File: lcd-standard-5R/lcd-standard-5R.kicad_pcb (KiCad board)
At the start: 4 copper layers, 137.4 x 82.6 mm, 156 parts, among them J1 USB_C_Receptacle_USB2.0_16P, J2 SWD, J3 Conn_ARM_JTAG_SWD_10, J4 Micro_SD_Card_Det1, J6 Conn_01x40_MountingPin, J7 Conn_01x02_MountingPin, J8 Serial, Q1 DMG3415, Q2 MMBT3904, Q3 MMBT3904, Q4 MMBT3904, SW1 SW_Push, SW2 SW_Push, SW3 BOOT0, SW4 RST, U1 siplex-som-s16, U2 AMS1117-3.3, U3 STM32H743ZITx, U4 MT48LC16M16A2P, U5 MT25Q, U6 CAT24C256, U7 XPT2046TS, U8 TPS61169, U9 MAX98357A, Y1 25MHz, Y2 32.768KHz

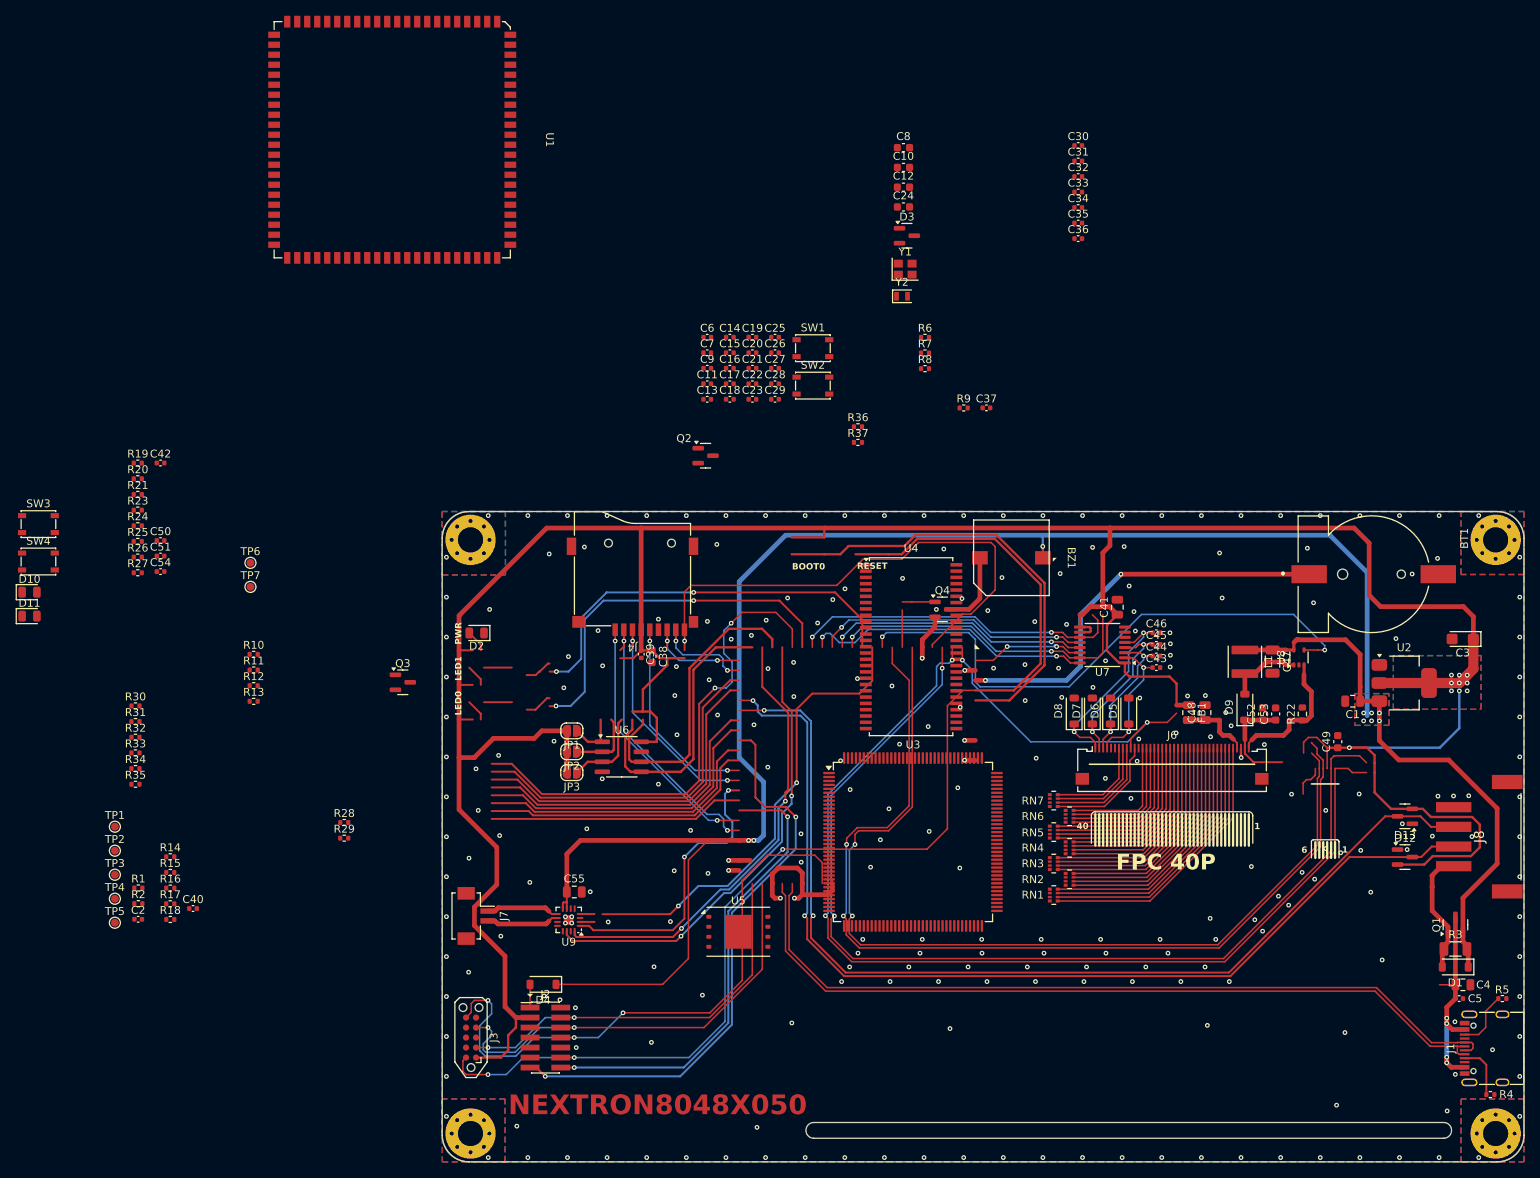
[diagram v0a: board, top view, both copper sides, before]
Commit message: Change MCU to STM32H743
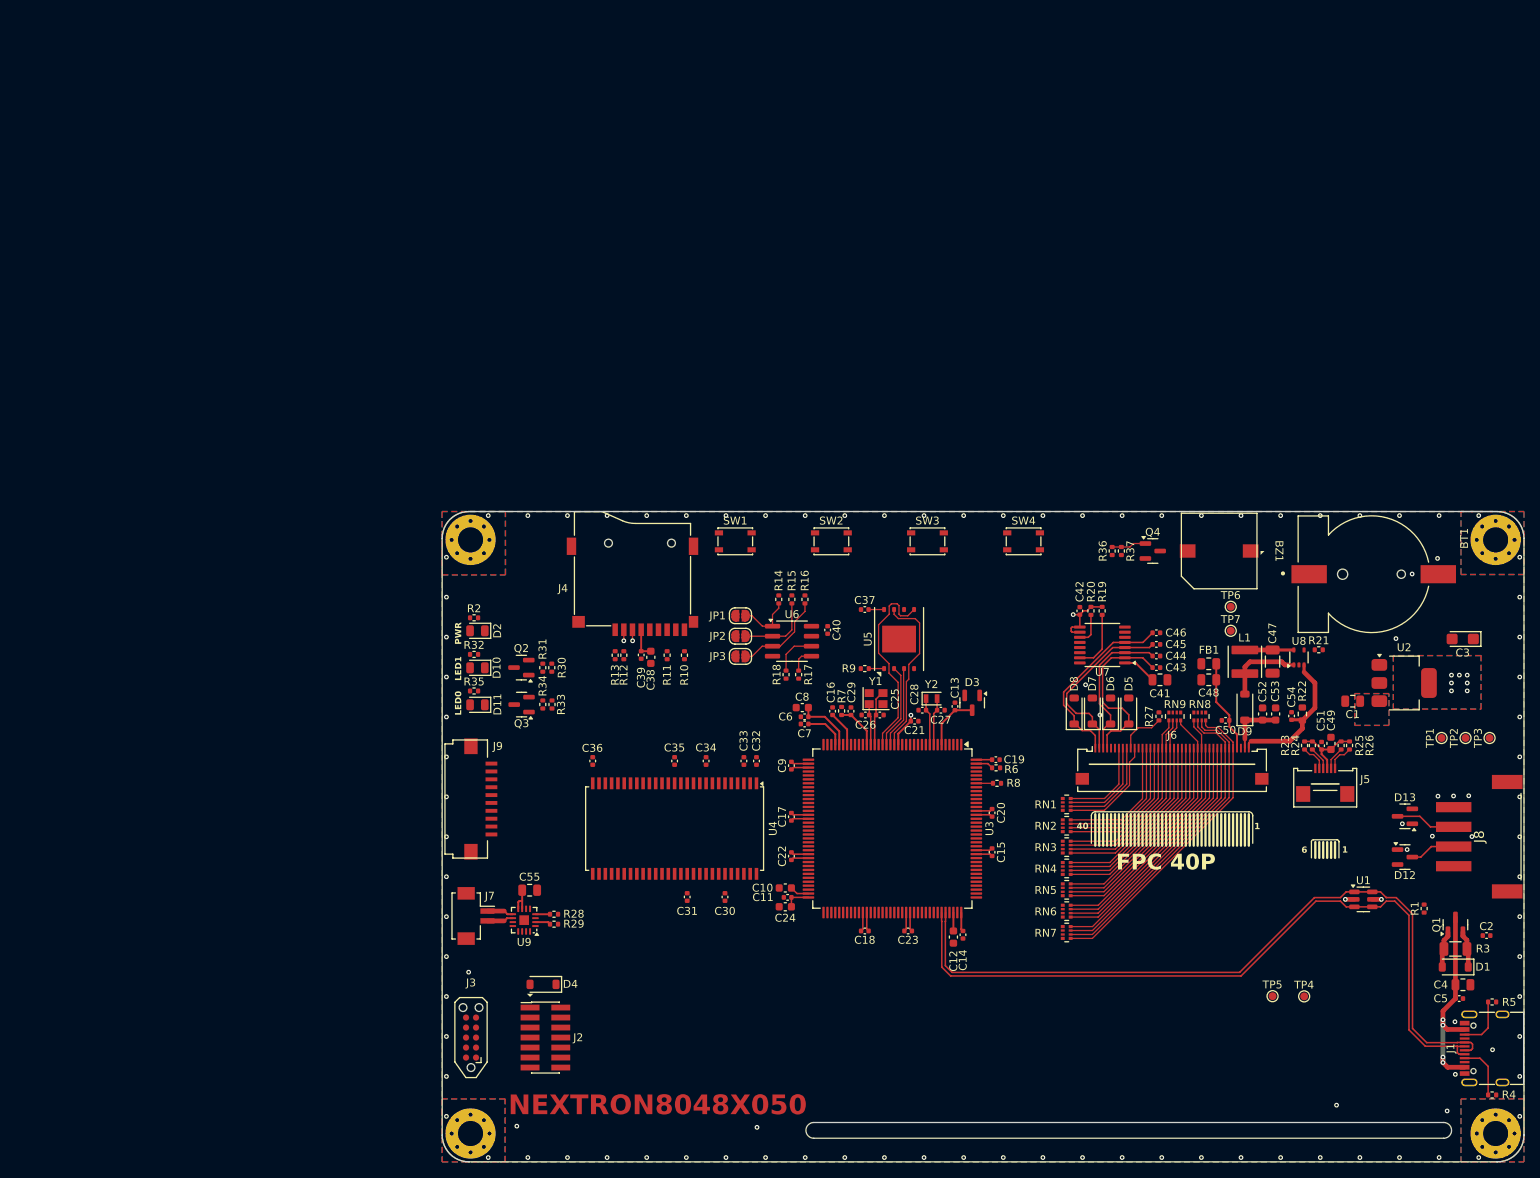
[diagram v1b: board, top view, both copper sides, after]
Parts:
- added J5: Conn_01x06_MountingPin, Connector_FPC:Conn_FPC_6P_0.5mm_XUNPU_FPC-05FB-6PH20, F.Cu at (188.6, 86.5)
- added J9: AUX_IO, Connector_FPC:Conn_FPC_10P_1mm_G-SWITCH_GT-F1008SR20-10SMT01, F.Cu at (82.7, 90.4)
- added RN8: 10K, Resistor_SMD:R_Array_Convex_4x0402, F.Cu at (172.6, 79.9)
- added RN9: 10K, Resistor_SMD:R_Array_Convex_4x0402, F.Cu at (169.5, 79.9)
- U1: value siplex-som-s16 -> USBLC6-2SC6; footprint siplex:siplex-som-s16 -> Package_TO_SOT_SMD:SOT-23-6
- moved TP3 175.5 mm to (209.5, 82.7), turned to 90 degrees
- moved TP2 172.1 mm to (206.4, 82.7), turned to 90 degrees
- moved C2 171.3 mm to (209.1, 107.8)
- moved TP1 168.9 mm to (203.4, 82.7), turned to 90 degrees
- moved R1 163.3 mm to (201.1, 104.3), turned to 90 degrees
- moved U1 156.6 mm to (193.4, 103.2), turned to 0 degrees
- moved R26 155.8 mm to (191.7, 83.6), turned to -90 degrees
- moved R25 155.0 mm to (190.6, 83.6), turned to -90 degrees
- moved R24 151.8 mm to (186.9, 83.6), turned to 90 degrees
- moved TP4 151.6 mm to (185.9, 115.5)
- moved R21 151.3 mm to (187.8, 71.5)
- moved R23 151.2 mm to (186.0, 83.6), turned to 90 degrees
- moved C51 149.4 mm to (188.1, 83.7), turned to 90 degrees
- moved TP5 147.3 mm to (181.9, 115.5)
- moved C54 144.8 mm to (184.3, 79.9), turned to 90 degrees
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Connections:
- net /DISPLAY/TP_BUSY renamed /DISPLAY/RTP_BUSY
- net /DISPLAY/TP_CLK renamed /DISPLAY/RTP_CLK
- net /DISPLAY/TP_CS renamed /DISPLAY/RTP_CS
- net /DISPLAY/TP_IRQ renamed /DISPLAY/RTP_IRQ
- net /DISPLAY/TP_MISO renamed /DISPLAY/RTP_MISO
- net /DISPLAY/TP_MOSI renamed /DISPLAY/RTP_MOSI
- J1 pad A6: /USB_DP -> /MCU/USB_D+
- J1 pad A7: /USB_DN -> /MCU/USB_D-
- J1 pad B6: /USB_DP -> /MCU/USB_D+
- J1 pad B7: /USB_DN -> /MCU/USB_D-
- J4 pad 1: /MEMORY_SD_CARD/DAT2 -> /MEMORY_SD_CARD/SD_DAT2
- J4 pad 2: /MEMORY_SD_CARD/DAT3 -> /MEMORY_SD_CARD/SD_DAT3
- J4 pad 3: /MEMORY_SD_CARD/CMD -> /MEMORY_SD_CARD/SD_CMD
- J4 pad 5: /MEMORY_SD_CARD/CLK -> /MEMORY_SD_CARD/SD_CLK
- J4 pad 7: /MEMORY_SD_CARD/DAT0 -> /MEMORY_SD_CARD/SD_DAT0
- J4 pad 8: /MEMORY_SD_CARD/DAT1 -> /MEMORY_SD_CARD/SD_DAT1
- J6 pad 11: /DISPLAY/LCD_CLK -> Net-(J6-Pin_11)
- J6 pad 13: /DISPLAY/LCD_B7 -> Net-(J6-Pin_13)
- J6 pad 14: /DISPLAY/LCD_B6 -> Net-(J6-Pin_14)
- J6 pad 15: /DISPLAY/LCD_B5 -> Net-(J6-Pin_15)
- J6 pad 16: /DISPLAY/LCD_B4 -> Net-(J6-Pin_16)
- J6 pad 17: /DISPLAY/LCD_B3 -> Net-(J6-Pin_17)
- J6 pad 18: /DISPLAY/LCD_B2 -> /DISPLAY/B2
- J6 pad 19: /DISPLAY/LCD_B1 -> /DISPLAY/B1
- J6 pad 20: /DISPLAY/LCD_B0 -> /DISPLAY/B0
- J6 pad 21: /DISPLAY/LCD_G7 -> Net-(J6-Pin_21)
- J6 pad 22: /DISPLAY/LCD_G6 -> Net-(J6-Pin_22)
- J6 pad 23: /DISPLAY/LCD_G5 -> Net-(J6-Pin_23)
- J6 pad 24: /DISPLAY/LCD_G4 -> Net-(J6-Pin_24)
- J6 pad 25: /DISPLAY/LCD_G3 -> Net-(J6-Pin_25)
- J6 pad 26: /DISPLAY/LCD_G2 -> Net-(J6-Pin_26)
- J6 pad 27: /DISPLAY/LCD_G1 -> /DISPLAY/G1
- J6 pad 28: /DISPLAY/LCD_G0 -> /DISPLAY/G0
- J6 pad 29: /DISPLAY/LCD_R7 -> Net-(J6-Pin_29)
- J6 pad 30: /DISPLAY/LCD_R6 -> Net-(J6-Pin_30)
- J6 pad 31: /DISPLAY/LCD_R5 -> Net-(J6-Pin_31)
- J6 pad 32: /DISPLAY/LCD_R4 -> Net-(J6-Pin_32)
- J6 pad 33: /DISPLAY/LCD_R3 -> Net-(J6-Pin_33)
- J6 pad 34: /DISPLAY/LCD_R2 -> /DISPLAY/R2
- J6 pad 35: /DISPLAY/LCD_R1 -> /DISPLAY/R1
- J6 pad 36: /DISPLAY/LCD_R0 -> /DISPLAY/R0
- J6 pad 7: /DISPLAY/LCD_DE -> Net-(J6-Pin_7)
- J6 pad 8: /DISPLAY/LCD_VSYNC -> Net-(J6-Pin_8)
- J6 pad 9: /DISPLAY/LCD_HSYNC -> Net-(J6-Pin_9)
- R11 pad 2: /MEMORY_SD_CARD/DAT0 -> /MEMORY_SD_CARD/SD_DAT0
- R12 pad 2: /MEMORY_SD_CARD/CMD -> /MEMORY_SD_CARD/SD_CMD
- R13 pad 2: /MEMORY_SD_CARD/DAT3 -> /MEMORY_SD_CARD/SD_DAT3
- R23 pad 1: /DISPLAY/TP_INT -> /DISPLAY/CTP_INT
- R24 pad 1: /DISPLAY/TP_WAKE -> /DISPLAY/CTP_WAKE
- R25 pad 2: /DISPLAY/TP_SDA -> /DISPLAY/CTP_SDA
- R26 pad 2: /DISPLAY/TP_SCL -> /DISPLAY/CTP_SCL
- RN1 pad 1: /LCD_R0 -> /DISPLAY/LCD_DE
- RN1 pad 2: /LCD_R1 -> /DISPLAY/LCD_VSYNC
- RN1 pad 3: /LCD_R2 -> /DISPLAY/LCD_HSYNC
- RN1 pad 4: /LCD_R3 -> /DISPLAY/LCD_CLK
- RN1 pad 5: /R3 -> Net-(J6-Pin_11)
- RN1 pad 6: /R2 -> Net-(J6-Pin_9)
- RN1 pad 7: /R1 -> Net-(J6-Pin_8)
- RN1 pad 8: Net-(RN1-R1.2) -> Net-(J6-Pin_7)
- RN2 pad 1: /LCD_R4 -> Net-(J6-Pin_16)
- RN2 pad 2: /LCD_R5 -> Net-(J6-Pin_15)
- RN2 pad 3: /LCD_R6 -> Net-(J6-Pin_14)
- RN2 pad 4: /LCD_R7 -> Net-(J6-Pin_13)
- RN2 pad 5: /R7 -> /DISPLAY/LCD_B7
- RN2 pad 6: /R6 -> /DISPLAY/LCD_B6
- RN2 pad 7: /R5 -> /DISPLAY/LCD_B5
- RN2 pad 8: /R4 -> /DISPLAY/LCD_B4
- RN3 pad 1: /LCD_G0 -> /DISPLAY/B0
- RN3 pad 2: /LCD_G1 -> /DISPLAY/B1
- RN3 pad 3: /LCD_G2 -> /DISPLAY/B2
- RN3 pad 4: /LCD_G3 -> Net-(J6-Pin_17)
- RN3 pad 5: /G3 -> /DISPLAY/LCD_B3
- RN3 pad 6: /G2 -> /DISPLAY/LCD_B2
- RN3 pad 7: /G1 -> /DISPLAY/LCD_B1
- RN3 pad 8: /G0 -> /DISPLAY/LCD_B0
- RN4 pad 1: /LCD_G4 -> Net-(J6-Pin_24)
- RN4 pad 2: /LCD_G5 -> Net-(J6-Pin_23)
- RN4 pad 3: /LCD_G6 -> Net-(J6-Pin_22)
- RN4 pad 4: /LCD_G7 -> Net-(J6-Pin_21)
- RN4 pad 5: /G7 -> /DISPLAY/LCD_G7
- RN4 pad 6: /G6 -> /DISPLAY/LCD_G6
- RN4 pad 7: /G5 -> /DISPLAY/LCD_G5
- RN4 pad 8: /G4 -> /DISPLAY/LCD_G4
- RN5 pad 1: /LCD_B0 -> /DISPLAY/G0
- RN5 pad 2: /LCD_B1 -> /DISPLAY/G1
- RN5 pad 3: /LCD_B2 -> Net-(J6-Pin_26)
- RN5 pad 4: /LCD_B3 -> Net-(J6-Pin_25)
- RN5 pad 5: /B3 -> /DISPLAY/LCD_G3
- RN5 pad 6: /B2 -> /DISPLAY/LCD_G2
- RN5 pad 7: /B1 -> /DISPLAY/LCD_G1
- RN5 pad 8: /B0 -> /DISPLAY/LCD_G0
- RN6 pad 1: /LCD_B4 -> Net-(J6-Pin_32)
- RN6 pad 2: /LCD_B5 -> Net-(J6-Pin_31)
- RN6 pad 3: /LCD_B6 -> Net-(J6-Pin_30)
- RN6 pad 4: /LCD_B7 -> Net-(J6-Pin_29)
- RN6 pad 5: /B7 -> /DISPLAY/LCD_R7
- RN6 pad 6: /B6 -> /DISPLAY/LCD_R6
- RN6 pad 7: /B5 -> /DISPLAY/LCD_R5
- RN6 pad 8: /B4 -> /DISPLAY/LCD_R4
- RN7 pad 1: /LCD_CLK -> /DISPLAY/R0
- RN7 pad 2: /LCD_HSYNC -> /DISPLAY/R1
- RN7 pad 3: /LCD_VSYNC -> /DISPLAY/R2
- RN7 pad 4: /LCD_DE -> Net-(J6-Pin_33)
- RN7 pad 5: Net-(RN7-R4.2) -> /DISPLAY/LCD_R3
- RN7 pad 6: Net-(RN7-R3.2) -> /DISPLAY/LCD_R2
- RN7 pad 7: Net-(RN7-R2.2) -> /DISPLAY/LCD_R1
- RN7 pad 8: Net-(RN7-R1.2) -> /DISPLAY/LCD_R0
- U1 pad 1: /LCD_RST -> /MCU/USB_D+
- U1 pad 2: /TP_SCL -> GND
- U1 pad 3: /TP_SDA -> /MCU/USB_D-
- U1 pad 4: /SD_DET -> /MCU/USB_D-
- U1 pad 5: GND -> VBUS
- U1 pad 6: /TP_INT -> /MCU/USB_D+
- U3 pad 123: /MCU/SD_CMD -> /MEMORY_SD_CARD/SD_CMD
- U3 pad 133: /MCU/SD_DAT2 -> /MEMORY_SD_CARD/SD_DAT2
- U3 pad 134: /MCU/SD_DAT3 -> /MEMORY_SD_CARD/SD_DAT3
- U3 pad 135: /MCU/SD_DET -> /MEMORY_SD_CARD/SD_DET
- U3 pad 136: /MCU/~{NOR_CS} -> /MEMORY_FLASH/~{NOR_CS}
- U3 pad 18: /MCU/NOR_D3 -> /MEMORY_FLASH/NOR_IO3
- U3 pad 19: /MCU/NOR_D2 -> /MEMORY_FLASH/NOR_IO2
- U3 pad 20: /MCU/NOR_D0 -> /MEMORY_FLASH/NOR_DO(IO1)
- U3 pad 21: /MCU/NOR_D1 -> /MEMORY_FLASH/NOR_DI(IO0)
- U3 pad 22: /MCU/LTDC_DE -> /DISPLAY/LCD_DE
- U3 pad 27: /MCU/SD_CLK -> /MEMORY_SD_CARD/SD_CLK
- U3 pad 3: /MCU/LCD_RESET -> /DISPLAY/LCD_RST
- U3 pad 40: /MCU/LTDC_VSYNC -> /DISPLAY/LCD_VSYNC
- U3 pad 43: /MCU/LCD_BLK -> /DISPLAY/LCD_BLK
- U3 pad 48: /MCU/NOR_CLK -> /MEMORY_FLASH/NOR_CLK
- U3 pad 75: /MCU/SD_DAT0 -> /MEMORY_SD_CARD/SD_DAT0
- U3 pad 76: /MCU/SD_DAT1 -> /MEMORY_SD_CARD/SD_DAT1
- U3 pad 92: /MCU/LTDC_CLK -> /DISPLAY/LCD_CLK
- U3 pad 96: /MCU/LTDC_HSYNC -> /DISPLAY/LCD_HSYNC
- U4 pad 10: /MEMORY_FMC/SDRAM_DQ5 -> /MCU/SDRAM_DQ5
- U4 pad 11: /MEMORY_FMC/SDRAM_DQ6 -> /MCU/SDRAM_DQ6
- U4 pad 13: /MEMORY_FMC/SDRAM_DQ7 -> /MCU/SDRAM_DQ7
- U4 pad 15: /MEMORY_FMC/SDRAM_LDQM -> /MCU/SDRAM_LDQM
- U4 pad 16: /MEMORY_FMC/~{SDRAM_WE} -> /MCU/~{SDRAM_WE}
- U4 pad 17: /MEMORY_FMC/~{SDRAM_CAS} -> /MCU/~{SDRAM_CAS}
- U4 pad 18: /MEMORY_FMC/~{SDRAM_RAS} -> /MCU/~{SDRAM_RAS}
- U4 pad 19: /MEMORY_FMC/~{SDRAM_CS} -> /MCU/~{SDRAM_CS}
- U4 pad 2: /MEMORY_FMC/SDRAM_DQ0 -> /MCU/SDRAM_DQ0
- U4 pad 20: /MEMORY_FMC/SDRAM_BA0 -> /MCU/SDRAM_BA0
- U4 pad 21: /MEMORY_FMC/SDRAM_BA1 -> /MCU/SDRAM_BA1
- U4 pad 22: /MEMORY_FMC/SDRAM_ADD10 -> /MCU/SDRAM_ADD10
- U4 pad 23: /MEMORY_FMC/SDRAM_ADD0 -> /MCU/SDRAM_ADD0
- U4 pad 24: /MEMORY_FMC/SDRAM_ADD1 -> /MCU/SDRAM_ADD1
- U4 pad 25: /MEMORY_FMC/SDRAM_ADD2 -> /MCU/SDRAM_ADD2
- U4 pad 26: /MEMORY_FMC/SDRAM_ADD3 -> /MCU/SDRAM_ADD3
- U4 pad 29: /MEMORY_FMC/SDRAM_ADD4 -> /MCU/SDRAM_ADD4
- U4 pad 30: /MEMORY_FMC/SDRAM_ADD5 -> /MCU/SDRAM_ADD5
- U4 pad 31: /MEMORY_FMC/SDRAM_ADD6 -> /MCU/SDRAM_ADD6
- U4 pad 32: /MEMORY_FMC/SDRAM_ADD7 -> /MCU/SDRAM_ADD7
- U4 pad 33: /MEMORY_FMC/SDRAM_ADD8 -> /MCU/SDRAM_ADD8
- U4 pad 34: /MEMORY_FMC/SDRAM_ADD9 -> /MCU/SDRAM_ADD9
- U4 pad 35: /MEMORY_FMC/SDRAM_ADD11 -> /MCU/SDRAM_ADD11
- U4 pad 36: /MEMORY_FMC/SDRAM_ADD12 -> /MCU/SDRAM_ADD12
- U4 pad 37: /MEMORY_FMC/SDRAM_CKE -> /MCU/SDRAM_CKE
- U4 pad 38: /MEMORY_FMC/SDRAM_CLK -> /MCU/SDRAM_CLK
- U4 pad 39: /MEMORY_FMC/SDRAM_UDQM -> /MCU/SDRAM_UDQM
- U4 pad 4: /MEMORY_FMC/SDRAM_DQ1 -> /MCU/SDRAM_DQ1
- U4 pad 42: /MEMORY_FMC/SDRAM_DQ8 -> /MCU/SDRAM_DQ8
- U4 pad 44: /MEMORY_FMC/SDRAM_DQ9 -> /MCU/SDRAM_DQ9
- U4 pad 45: /MEMORY_FMC/SDRAM_DQ10 -> /MCU/SDRAM_DQ10
- U4 pad 47: /MEMORY_FMC/SDRAM_DQ11 -> /MCU/SDRAM_DQ11
- U4 pad 48: /MEMORY_FMC/SDRAM_DQ12 -> /MCU/SDRAM_DQ12
- U4 pad 5: /MEMORY_FMC/SDRAM_DQ2 -> /MCU/SDRAM_DQ2
- U4 pad 50: /MEMORY_FMC/SDRAM_DQ13 -> /MCU/SDRAM_DQ13
- U4 pad 51: /MEMORY_FMC/SDRAM_DQ14 -> /MCU/SDRAM_DQ14
- U4 pad 53: /MEMORY_FMC/SDRAM_DQ15 -> /MCU/SDRAM_DQ15
- U4 pad 7: /MEMORY_FMC/SDRAM_DQ3 -> /MCU/SDRAM_DQ3
- U4 pad 8: /MEMORY_FMC/SDRAM_DQ4 -> /MCU/SDRAM_DQ4
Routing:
- net +3V3: track 410.3 -> 73.3 mm, vias 10 -> 9
- net VDD: track 279.0 -> 14.7 mm, vias 9 -> 0
- net /RESET: track 153.2 -> 0.00 mm, vias 3 -> 0
- net /TP_SCL: track 130.6 -> 0.00 mm, vias 2 -> 0
- net /TP_SDA: track 130.0 -> 0.00 mm, vias 2 -> 0
- net /TP_WAKE: track 123.5 -> 0.00 mm, vias 2 -> 0
- net /IO/SERIAL_TX: track 128.9 -> 5.81 mm, vias 2 -> 0
- net /IO/SERIAL_RX: track 129.7 -> 7.68 mm, vias 2 -> 0
- net /TP_INT: track 119.7 -> 0.00 mm, vias 2 -> 0
- net /USB_DP: track 102.1 -> 0.00 mm
- net /USB_DN: track 101.8 -> 0.00 mm
- net /MCU/USB_D+: track 0.00 -> 96.5 mm
- net /MCU/USB_D-: track 0.00 -> 96.3 mm
- net /MEMORY_FMC/SDRAM_UDQM: track 88.1 -> 0.00 mm
- net /MEMORY_FMC/SDRAM_CLK: track 79.1 -> 0.00 mm
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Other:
- board text removed: "BOOT0"
- board text removed: "RESET"

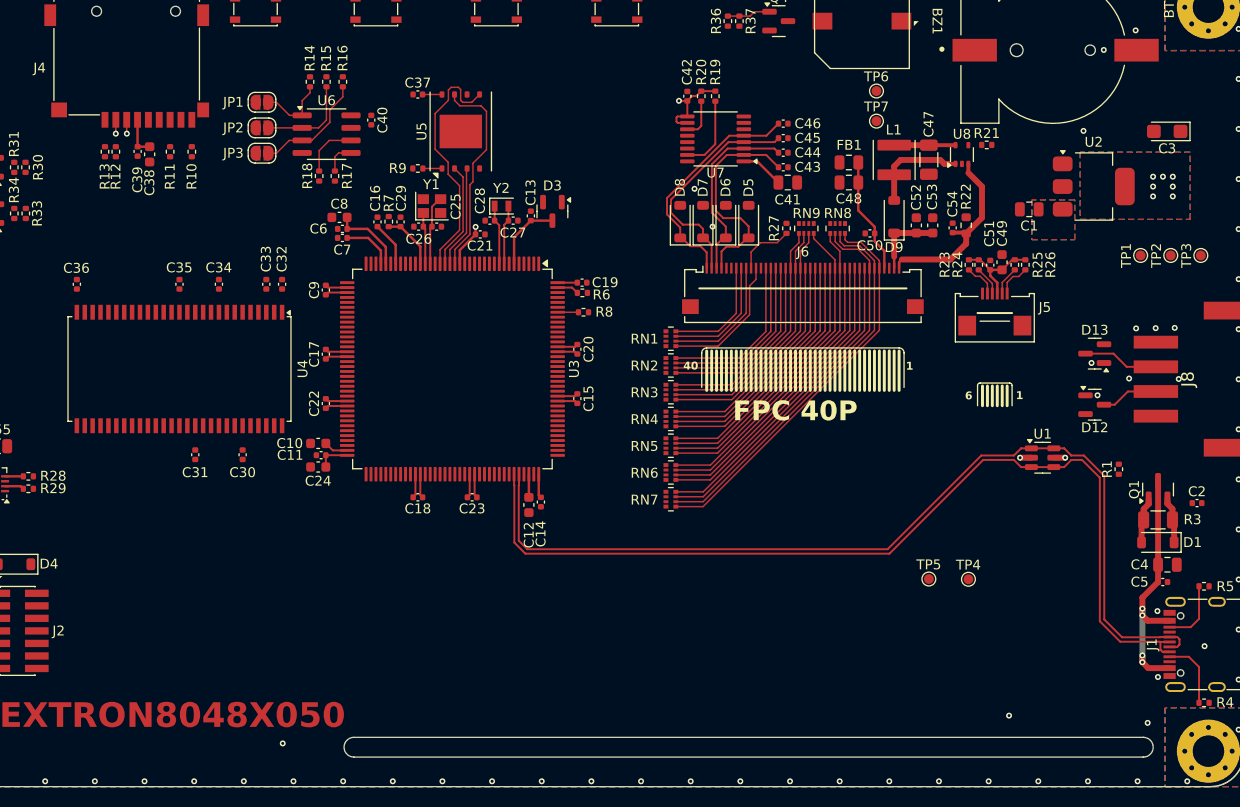
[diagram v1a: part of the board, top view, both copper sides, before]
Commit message: Add 10P FPC for 5-inch Tailor pixel CTP
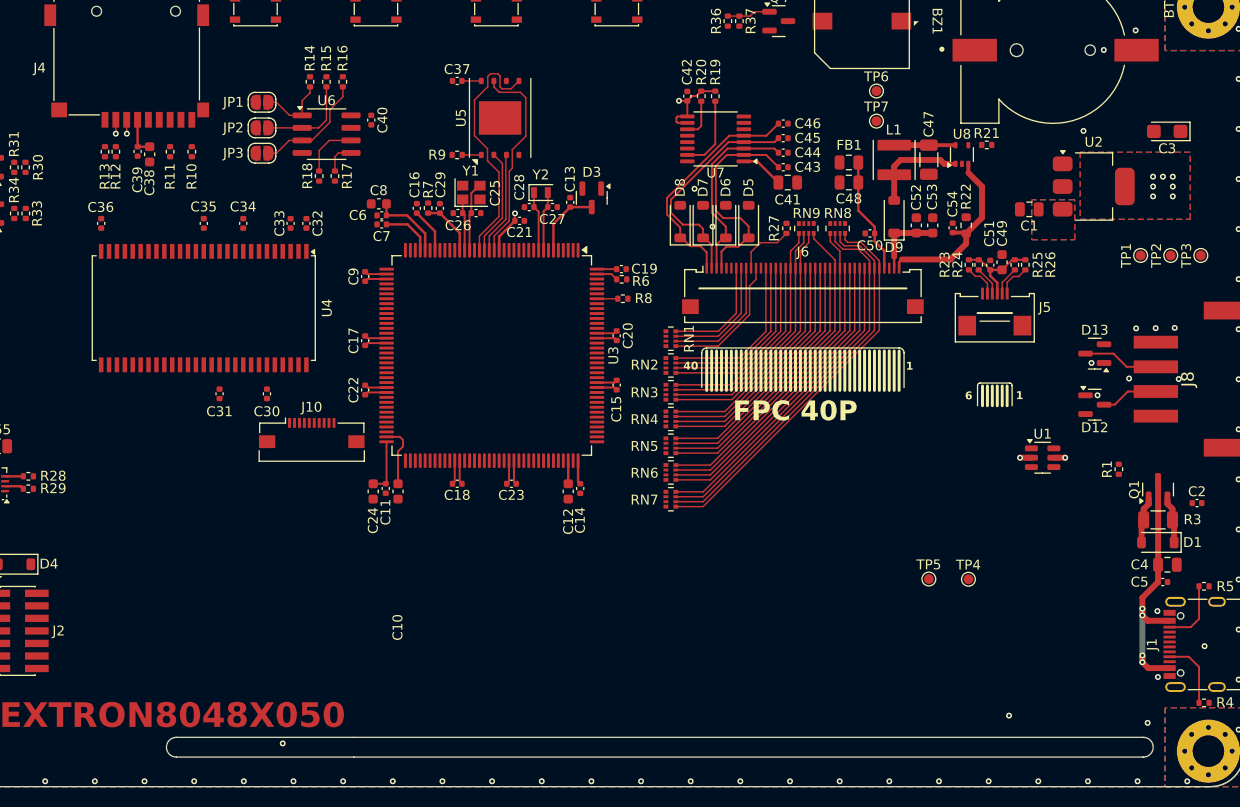
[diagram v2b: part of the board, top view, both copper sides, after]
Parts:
- added J10: Conn_01x10_MountingPin, Connector_FFC-FPC:Molex_54548-1071_1x10-1MP_P0.5mm_Horizontal, F.Cu at (119.4, 100.7)
- moved C10 9.44 mm to (128.1, 106.6), turned to -90 degrees
- moved C11 7.37 mm to (126.8, 106.3), turned to -90 degrees
- moved C33 6.65 mm to (117.2, 79.4)
- moved C34 6.65 mm to (112.4, 79.4)
- moved C35 6.65 mm to (108.4, 79.4)
- moved U4 6.65 mm to (108.4, 88.0)
- moved C30 6.65 mm to (114.8, 96.7)
- moved C31 6.65 mm to (110.0, 96.7)
- moved C32 6.65 mm to (118.8, 79.4)
- moved C36 6.65 mm to (98.0, 79.4)
- moved C24 6.10 mm to (125.6, 106.6), turned to -90 degrees
- moved C21 4.22 mm to (140.4, 79.2)
- moved C25 4.22 mm to (136.0, 78.4)
- moved D3 4.22 mm to (147.7, 76.8)
- moved C12 4.22 mm to (145.3, 106.6)
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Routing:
- net /MCU/USB_D+: track 96.5 -> 0.00 mm
- net /MCU/USB_D-: track 96.3 -> 0.00 mm
- net Net-(C10-Pad1): track 4.80 -> 8.80 mm
- net +3V3: track 73.3 -> 75.5 mm
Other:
- outline, holes or cut-outs redrawn
